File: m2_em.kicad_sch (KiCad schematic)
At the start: 0 parts

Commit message: Finished part of the M.2. schematic capture
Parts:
- added C49, C50: 220nF/50V, symbol Device:C_Small
- added C51, C52, C53, C57, C58, C59: 10uF/10v, symbol Device:C
- added C54, C60: 100uF/10v, symbol Device:C
- added D9: LED, symbol Device:LED
- added J80: Bus_M.2_Socket_M, symbol Connector:Bus_M.2_Socket_M
- added J81: Bus_M.2_Socket_E, symbol Connector:Bus_M.2_Socket_E
- added R27, R29: 0R/1%, symbol Device:R
- added R30, R31: 2.2K/1%, symbol Device:R
- added TP2: TestPoint, symbol Connector:TestPoint
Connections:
- new net: C50.2, J80.47 (PETn0/SATA-A-)
- new net: J80.69 (PEDET), R31.1
- new net: D9.2 (A), R30.2
- new net: D9.1 (K), J80.10 (DAS/~{DSS}/~{LED1})
- new net: J80.38 (DEVSLP), TP2.1
- new net: C49.2, J80.49 (PETp0/SATA-A+)
- new net: J80.68 (SUSCLK), R29.1
- new net +3.3V: C51.1, C52.1, C53.1, C54.1, C57.1, C58.1, C59.1, C60.1, J80.12 (3.3V), J80.14 (3.3V), J80.16 (3.3V), J80.18 (3.3V), J80.2 (3.3V), J80.4 (3.3V), J80.70 (3.3V), J80.72 (3.3V), J80.74 (3.3V), J81.2 (3.3V), J81.4 (3.3V), J81.72 (3.3V), J81.74 (3.3V), R30.1
- new net CLKREQM: J80.52 (~{CLKREQ}), R27.2
- new net GND: C51.2, C52.2, C53.2, C54.2, C57.2, C58.2, C59.2, C60.2, J80.1 (GND), J80.15 (GND), J80.21 (GND), J80.27 (GND), J80.3 (GND), J80.33 (GND), J80.39 (GND), J80.45 (GND), J80.51 (GND), J80.57 (GND), J80.71 (GND), J80.73 (GND), J80.75 (GND), J80.9 (GND), J81.1 (GND), J81.18 (GND), J81.33 (GND), J81.39 (GND), J81.45 (GND), J81.51 (GND), J81.57 (GND), J81.63 (GND), J81.69 (GND), J81.7 (GND), J81.75 (GND), R27.1, R31.2
- new net PCIe_RX_1+: J80.43 (PERp0/SATA-B-)
- new net PCIe_RX_1-: J80.41 (PERn0/SATA-B+)
- new net PCIe_TX_1+: C49.1
- new net PCIe_TX_1-: C50.1
- new net REFCLKM+: J80.55 (REFCLKp)
- new net REFCLKM-: J80.53 (REFCLKn)
- new net SUSCLK: R29.2
- new net ~{PLT_RST}: J80.50 (~{PERST})
- new net ~{WAKE}: J80.54 (~{PEWAKE})
- no-connect marks 0 -> 49
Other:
- note added: "SSD active LED"
- note added: "To be grounded for SATA. No Connect for PCIe"

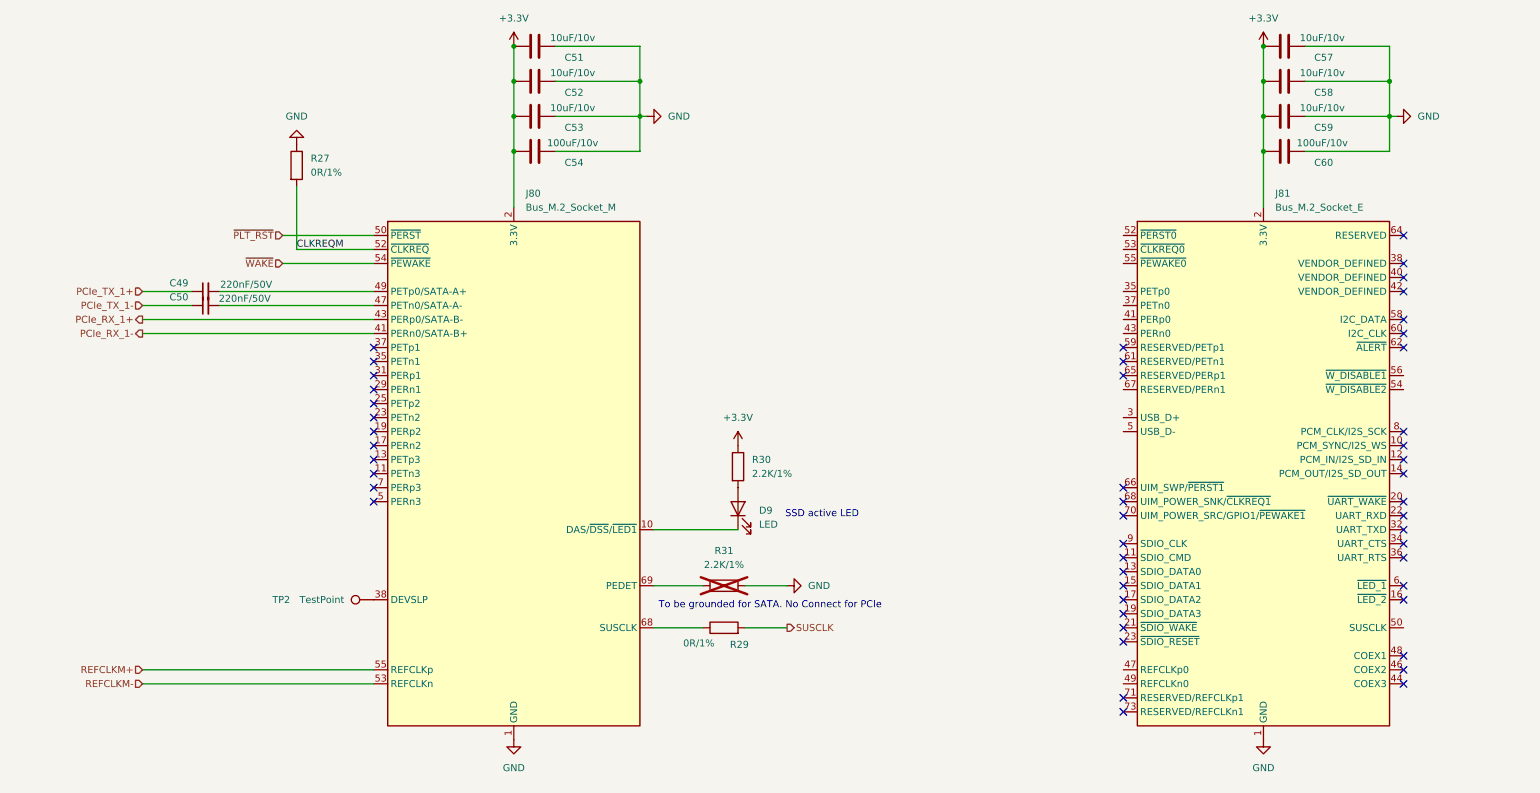
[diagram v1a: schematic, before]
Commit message: Finished the shematic capture of the M.2 sheet but still have to assign the footprints
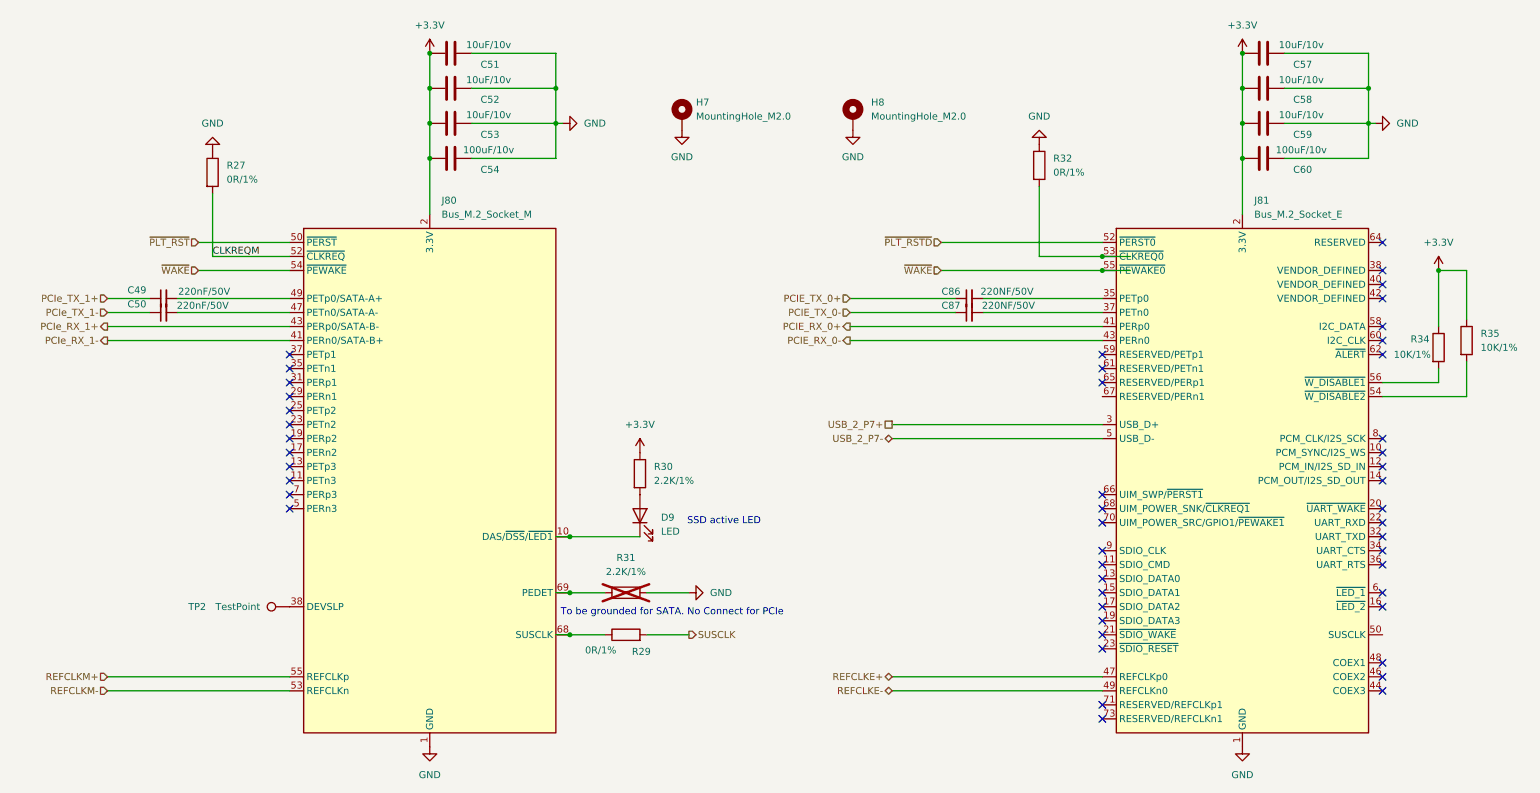
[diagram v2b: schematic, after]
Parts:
- added C86, C87: 220NF/50V, symbol Device:C_Small
- added H7, H8: MountingHole_M2.0, symbol Mechanical:MountingHole_Pad
- added R32: 0R/1%, symbol Device:R
- added R34, R35: 10K/1%, symbol Device:R
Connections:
- net +3.3V: now also R34.1, R35.1
- net GND: now also H7.1, H8.1, R32.1
- net ~{WAKE}: now also J81.55 (~{PEWAKE0})
- net USB_2_P7+: now reaches J81.3 (USB_D+)
- net at J81.35 (PETp0): now also C86.2
- net at J81.37 (PETn0): now also C87.2
- net PCIE_RX_0+: now reaches J81.41 (PERp0)
- net PCIE_RX_0-: now reaches J81.43 (PERn0)
- net REFCLKE+: now reaches J81.47 (REFCLKp0)
- net REFCLKE-: now reaches J81.49 (REFCLKn0)
- net USB_2_P7-: now reaches J81.5 (USB_D-)
- net ~{PLT_RSTD}: now reaches J81.52 (~{PERST0})
- net at J81.53 (~{CLKREQ0}): now also R32.2
- net at J81.54 (~{W_DISABLE2}): now also R35.2
- net at J81.56 (~{W_DISABLE1}): now also R34.2
- new net PCIE_TX_0+: C86.1
- new net PCIE_TX_0-: C87.1
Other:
- moved on the sheet: C49, C50, C51, C52, C53, C54, C57, C58, C59, C60, D9, J80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

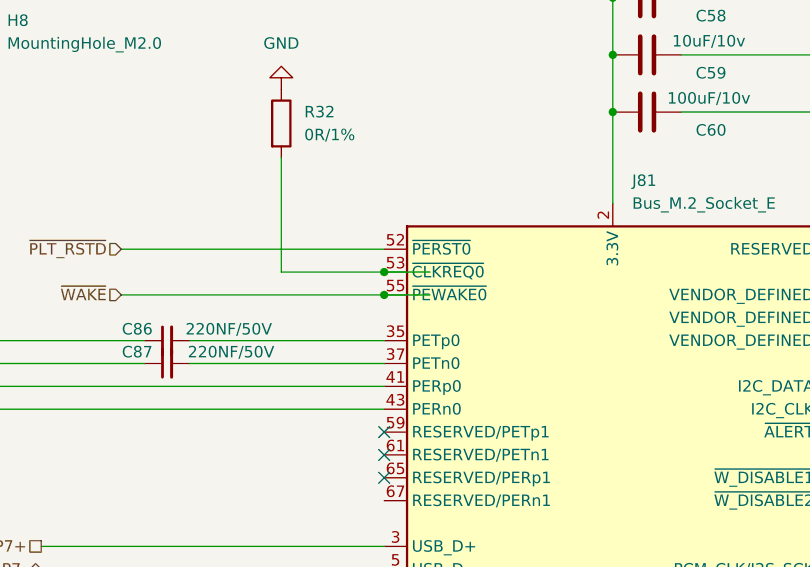
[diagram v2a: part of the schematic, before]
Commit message: Connected the usb sheets together in the the roor sheet
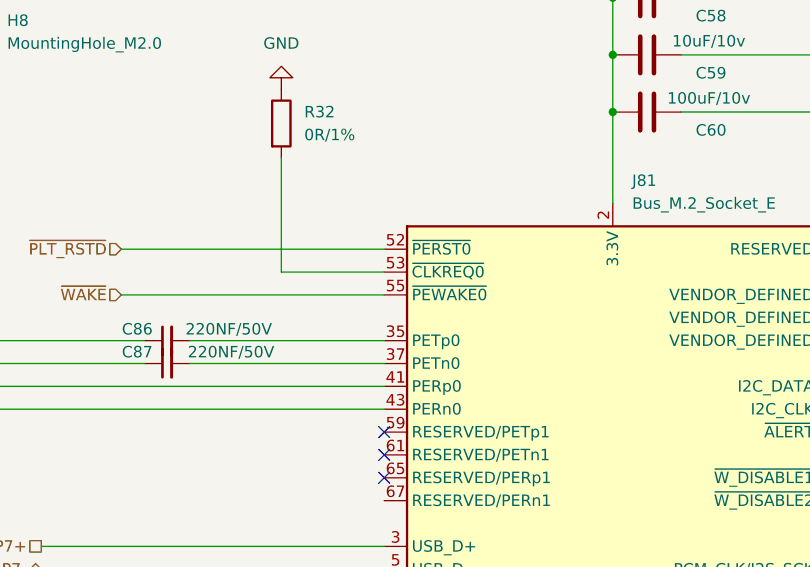
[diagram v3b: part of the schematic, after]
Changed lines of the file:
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@@
-	)
-	(junction
-		(at 208.28 69.85)
-		(diameter 0)
-		(color 0 0 0 0)
-	)
-	(junction
-		(at 208.28 67.31)
-		(diameter 0)
-		(color 0 0 0 0)
 	)
 	(junction
@@
 	(wire
 		(pts
-			(xy 213.36 69.85) (xy 208.28 69.85)
-		)
-		(stroke
-			(width 0)
-			(type default)
-		)
-	)
-	(wire
-		(pts
 			(xy 133.35 128.27) (xy 125.73 128.27)
 		)
@@
 		)
 		(stroke
-			(width 0)
-			(type default)
-		)
-	)
-	(wire
-		(pts
-			(xy 213.36 67.31) (xy 208.28 67.31)
-		)
-		(stroke

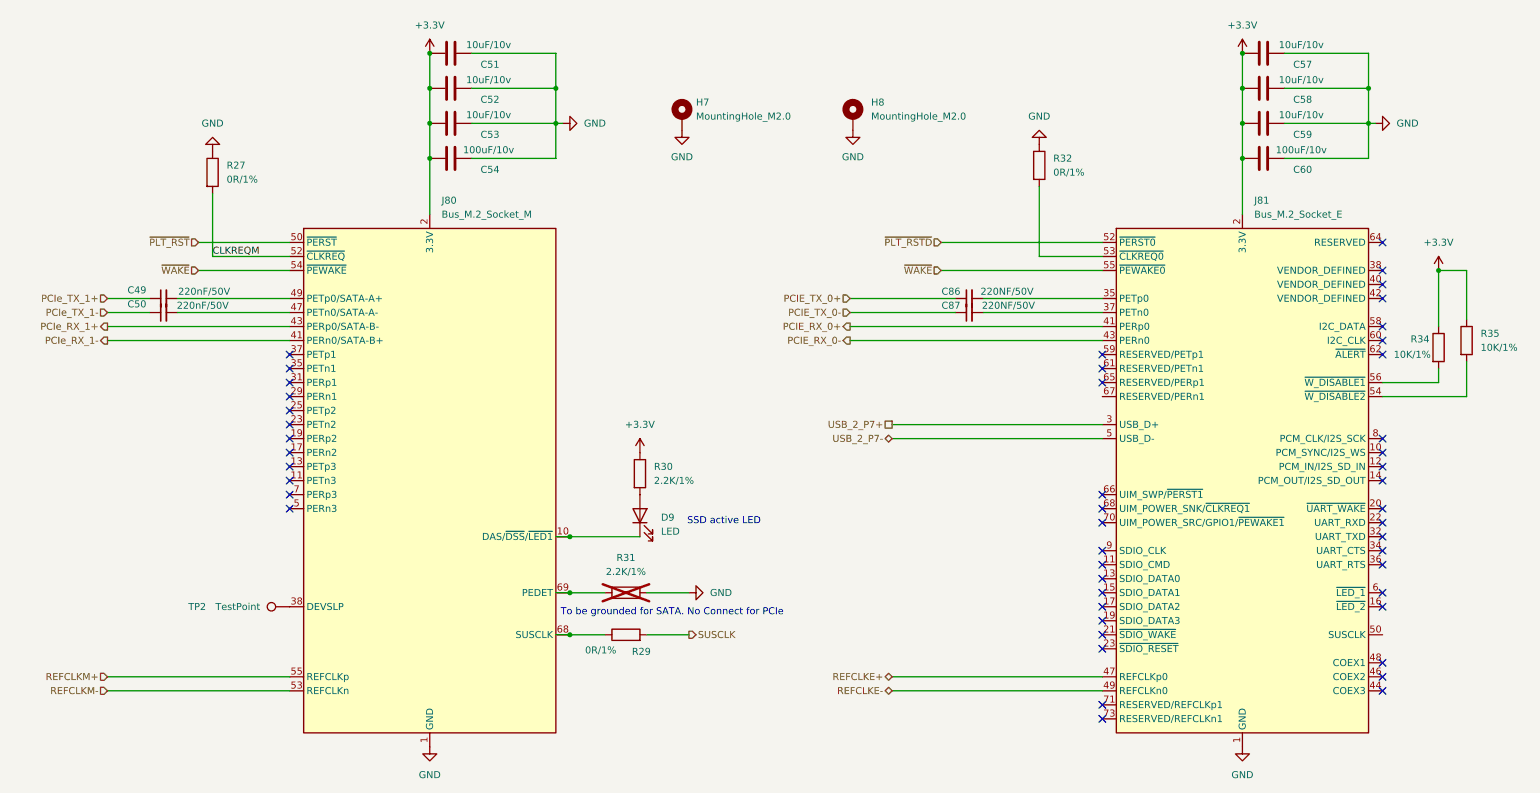
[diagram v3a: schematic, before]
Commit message: finished the entire schematic capture for each of the sub sheets .and then the next part is to .fix all the erc errors when impoting the shematic in to the pcb to get readu for routing
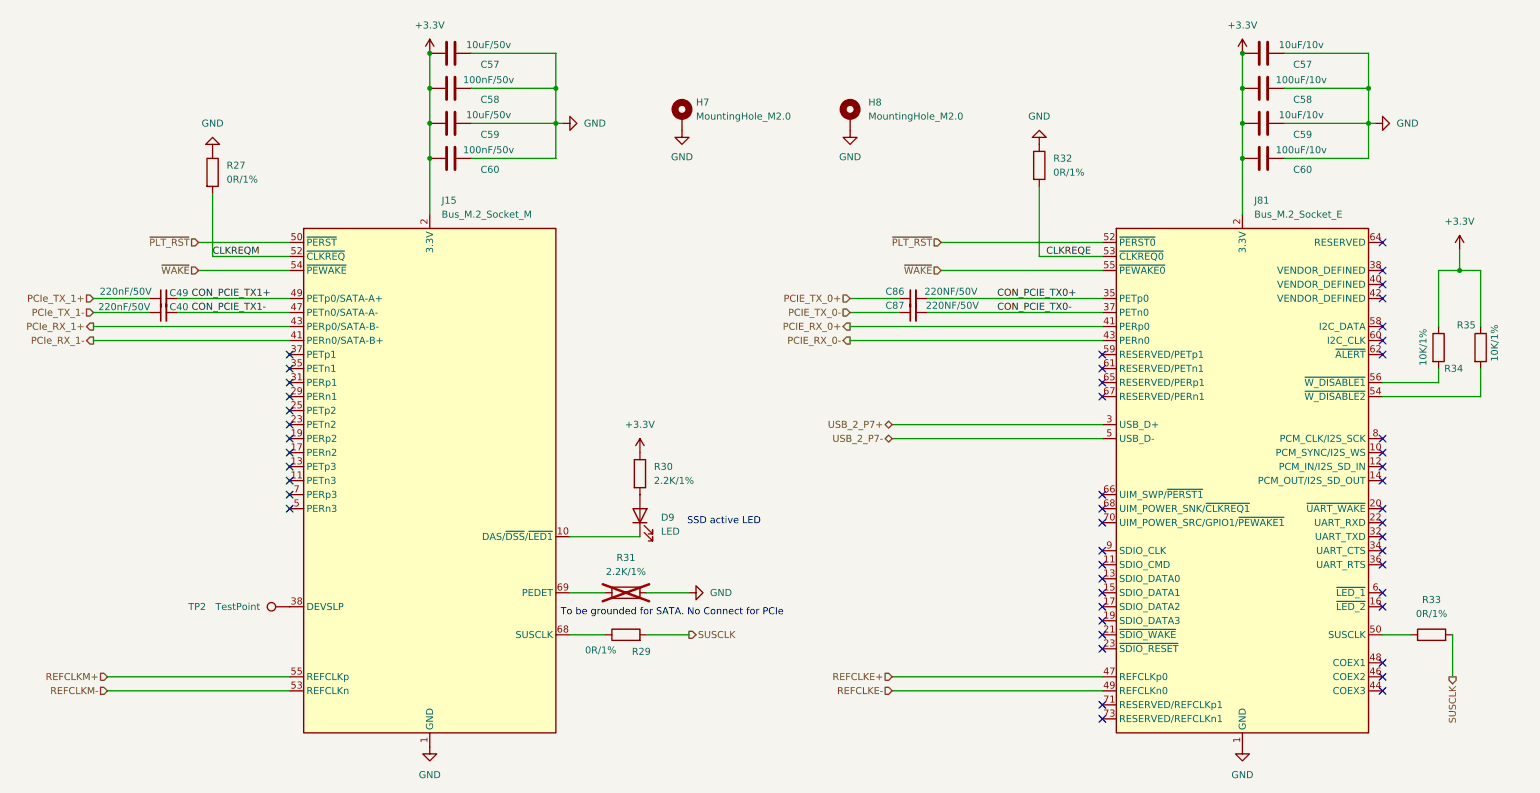
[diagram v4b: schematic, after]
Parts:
- added R33: 0R/1%, A_HDJ_Library:R_0402_1005Metric, symbol Device:R
- C40: renamed from C50; footprint (none) -> A_HDJ_Library:C_0402_1005Metric
- C49, C57, C59, C60, C86, C87: footprint (none) -> A_HDJ_Library:C_0402_1005Metric
- C57: renamed from C51; value 10uF/10v -> 10uF/50v; footprint (none) -> A_HDJ_Library:C_0402_1005Metric
- C58: renamed from C52; value 10uF/10v -> 100nF/50v; footprint (none) -> A_HDJ_Library:C_0402_1005Metric
- C58: value 10uF/10v -> 100uF/10v; footprint (none) -> A_HDJ_Library:C_0402_1005Metric
- C59: renamed from C53; value 10uF/10v -> 10uF/50v; footprint (none) -> A_HDJ_Library:C_0402_1005Metric
- C60: renamed from C54; value 100uF/10v -> 100nF/50v; footprint (none) -> A_HDJ_Library:C_0402_1005Metric
- J15: renamed from J80; footprint (none) -> A_HDJ_Library:PCIe_M.2_Connectors_P=0.5mm_H=4.2mm_KeyM
- J81: footprint (none) -> A_HDJ_Library:PCIe_M.2_Connectors_P=0.5mm_H=4.2mm_KeyE
- R27, R29, R30, R32, R34: footprint (none) -> A_HDJ_Library:R_0402_1005Metric
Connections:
- net ~{PLT_RSTD} is gone; now on net ~{PLT_RST}: J81.52 (~{PERST0})
- net SUSCLK: now also R33.2
- net CON_PCIE_TX1-: now reaches C40.2, J15.47 (PETn0/SATA-A-)
- net CON_PCIE_TX1+: now reaches C49.2, J15.49 (PETp0/SATA-A+)
- net CON_PCIE_TX0-: now reaches C87.2, J81.37 (PETn0)
- net CON_PCIE_TX0+: now reaches C86.2, J81.35 (PETp0)
- net at J81.50 (SUSCLK): now also R33.1
- net CLKREQE: now reaches J81.53 (~{CLKREQ0}), R32.2
- no-connect marks 49 -> 50
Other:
- moved on the sheet: C86, C87, H8, R35
